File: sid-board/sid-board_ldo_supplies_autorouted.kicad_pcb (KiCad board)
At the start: 2 copper layers, 39.5 x 40.8 mm, 17 parts, among them J1 ICM_CONN, J2 SID_CONN, J3 5V OUT, J4 3.3V OUT, J5 SPI, U1 SC16IS752IPW, U2 MCP1703A-33, U3 PCA82C250, U4 PCA82C250, U5 MCP1703A-5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

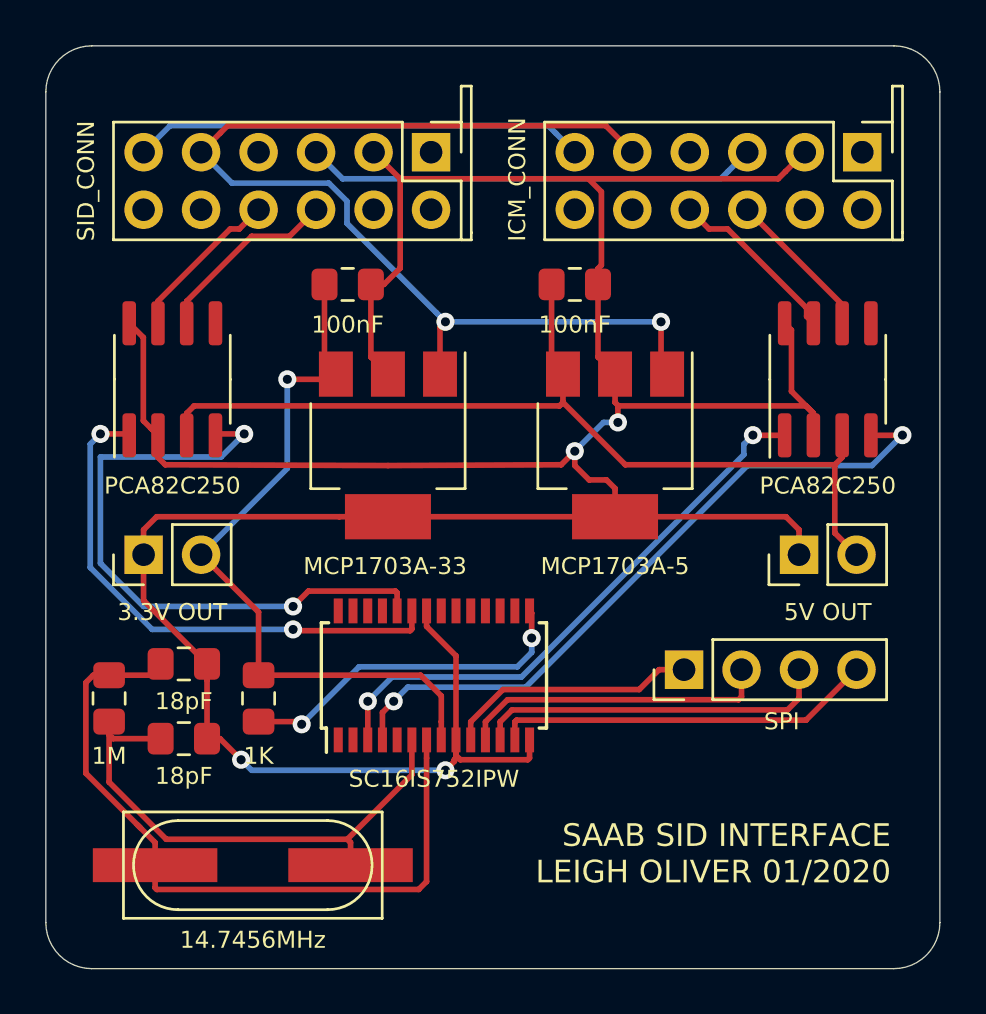
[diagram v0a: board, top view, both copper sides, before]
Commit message: Updated manually routed board, removed debugging UART header.
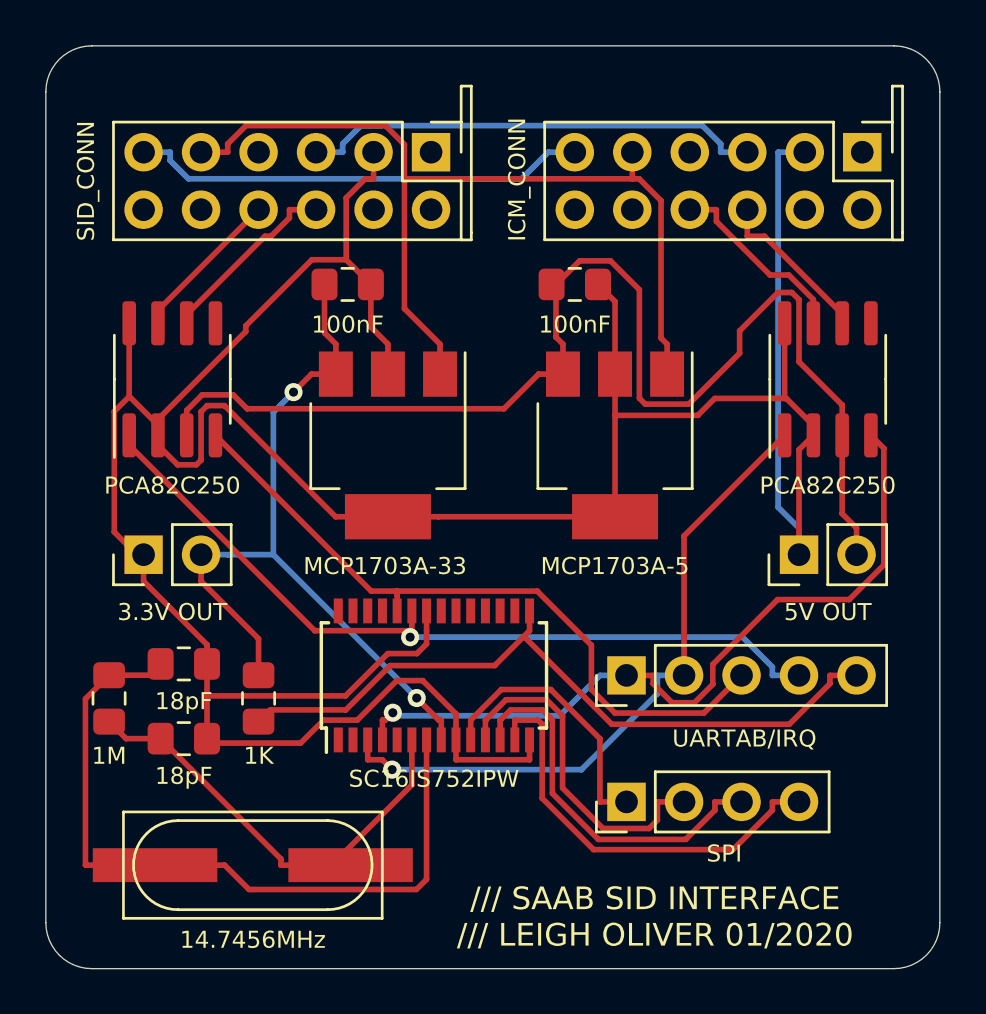
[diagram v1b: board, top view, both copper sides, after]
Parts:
- added J6: UARTAB/IRQ, Connector_PinHeader_2.54mm:PinHeader_1x05_P2.54mm_Vertical, F.Cu at (89.9, 87.4)
- moved J5 6.37 mm to (89.9, 93.0)
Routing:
- net Net-(J6-Pad5): track 15.3 -> 31.9 mm, vias 2 -> 0
- net VDD_5V: track 42.2 -> 54.9 mm
- net Net-(J6-Pad4): track 23.6 -> 35.6 mm, vias 2 -> 1
- net VIN: track 48.9 -> 41.5 mm, vias 2 -> 0
- net Net-(J6-Pad2): track 25.3 -> 29.7 mm, vias 2 -> 1
- net XTAL1: track 23.9 -> 20.5 mm
- net Net-(J6-Pad3): track 27.8 -> 31.0 mm, vias 2 -> 0
- net Net-(J6-Pad1): track 30.7 -> 33.7 mm, vias 2 -> 1
- net VDD_3.3V: track 32.5 -> 34.8 mm, vias 1 -> 2
- net Net-(J5-Pad4): track 16.8 -> 18.8 mm
- net Net-(J5-Pad2): track 13.8 -> 15.2 mm
- net Net-(J5-Pad3): track 15.7 -> 16.9 mm
- net GND: track 151.9 -> 151.0 mm, vias 4 -> 0
- net Net-(J5-Pad1): track 11.2 -> 12.0 mm
- net Net-(J1-Pad9): track 7.76 -> 8.45 mm
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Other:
- board text added: "/// SAAB SID INTERFACE /// LEIGH OLIVER 01/2020"
- board text removed: "SAAB SID INTERFACE LEIGH OLIVER 01/2020"

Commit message: Autorouted vs Manual routed. Thinking about adding DIP switch.
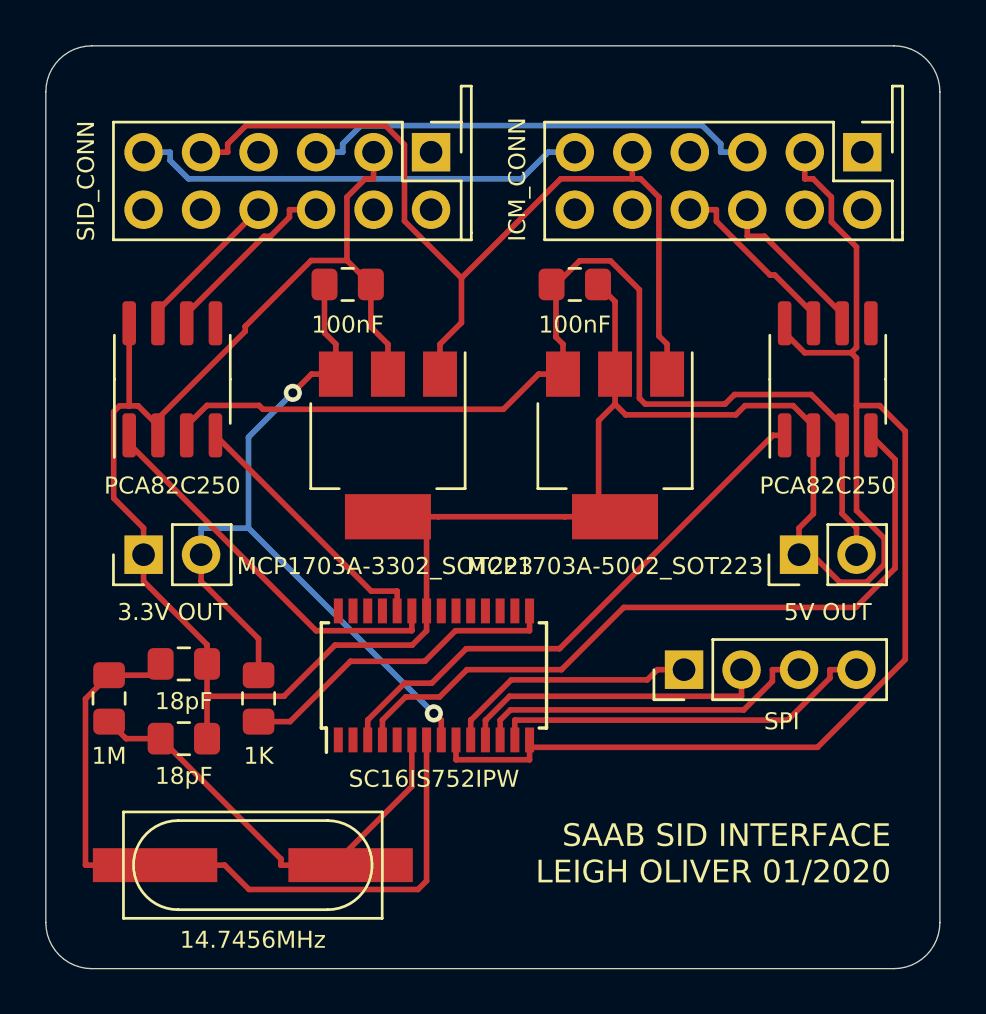
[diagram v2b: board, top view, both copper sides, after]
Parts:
- removed J6: UARTAB/IRQ, Connector_PinHeader_2.54mm:PinHeader_1x05_P2.54mm_Vertical
- U2: value MCP1703A-33 -> MCP1703A-3302_SOT223
- U5: value MCP1703A-5 -> MCP1703A-5002_SOT223
- moved J5 6.37 mm to (92.5, 87.1)
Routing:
- net Net-(U1-Pad24): track 31.0 -> 11.8 mm
- net Net-(U1-Pad23): track 35.6 -> 17.2 mm, vias 1 -> 0
- net Net-(R1-Pad1): track 31.9 -> 14.5 mm
- net GND: track 151.0 -> 162.3 mm
- net VDD_5V: track 54.9 -> 47.6 mm
- net Net-(U1-Pad3): track 29.7 -> 24.5 mm, vias 1 -> 0
- net Net-(J5-Pad4): track 18.8 -> 17.1 mm
- net Net-(J5-Pad3): track 16.9 -> 15.3 mm
- net Net-(J5-Pad2): track 15.2 -> 13.8 mm
- net Net-(U1-Pad4): track 33.7 -> 32.6 mm, vias 1 -> 0
- net VDD_3.3V: track 34.8 -> 35.8 mm
- net Net-(J5-Pad1): track 12.0 -> 11.2 mm
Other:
- board text added: "SAAB SID INTERFACE LEIGH OLIVER 01/2020"
- board text removed: "/// SAAB SID INTERFACE /// LEIGH OLIVER 01/2020"
